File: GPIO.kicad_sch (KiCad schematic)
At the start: 12 parts, among them J10 Conn_01x03_Pin, J11 Conn_01x03_Pin, J12 Conn_01x04_Pin, J13 Conn_01x04_Pin, J14 Conn_01x03_Pin, J78 I2C, J8 Conn_01x03_Pin, J80 I2C, U10 ULC0524P, U12 ULC0524P

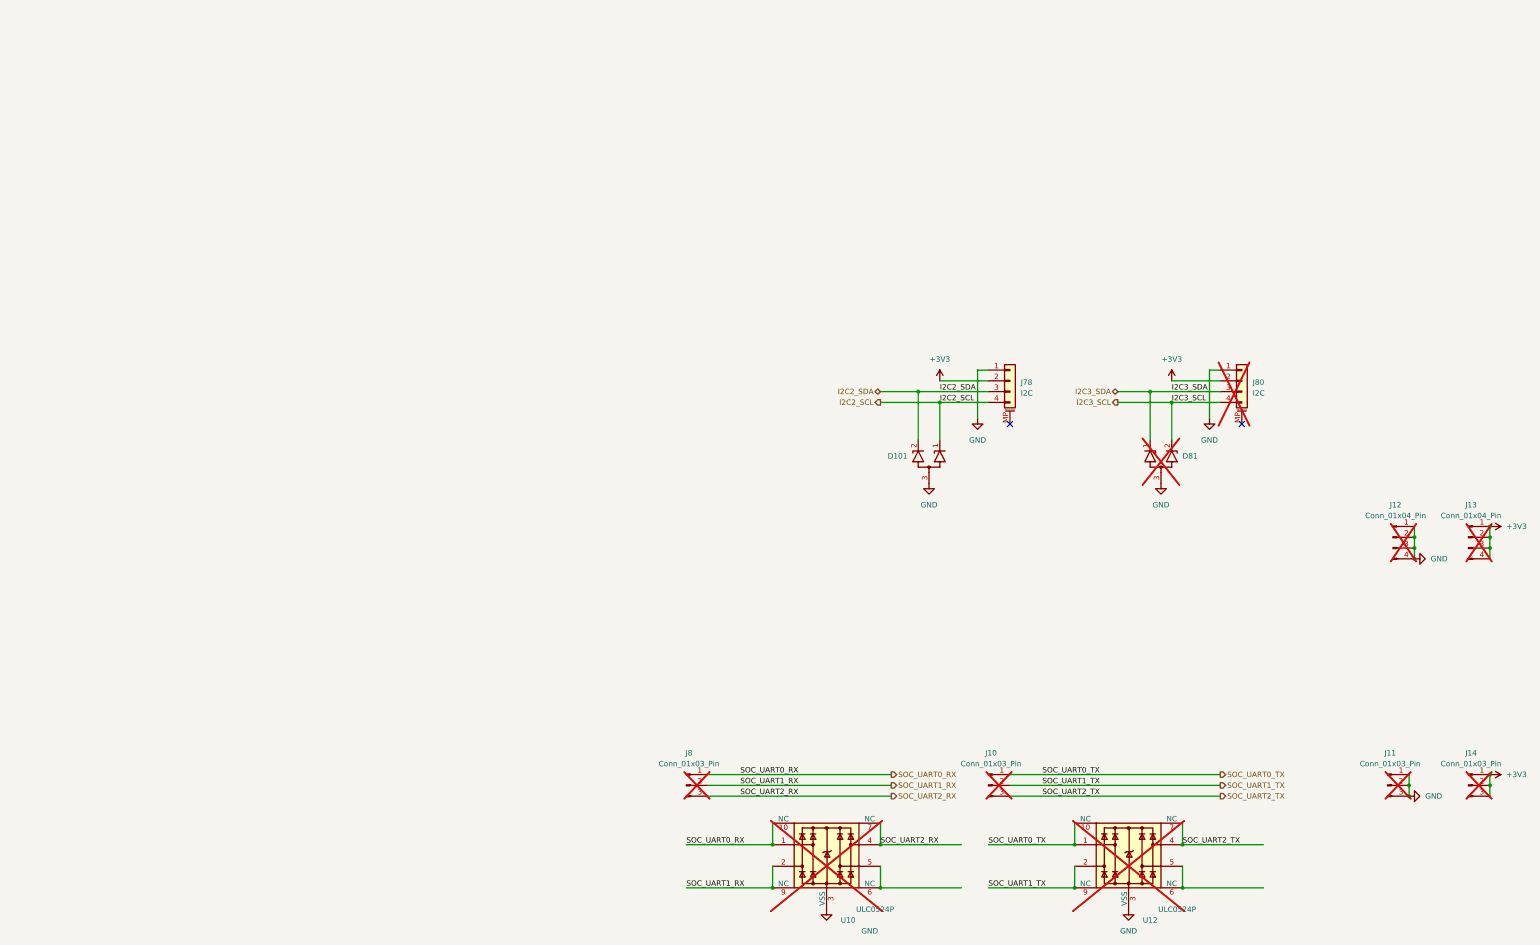
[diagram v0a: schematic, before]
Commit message: hierarchical schema rework
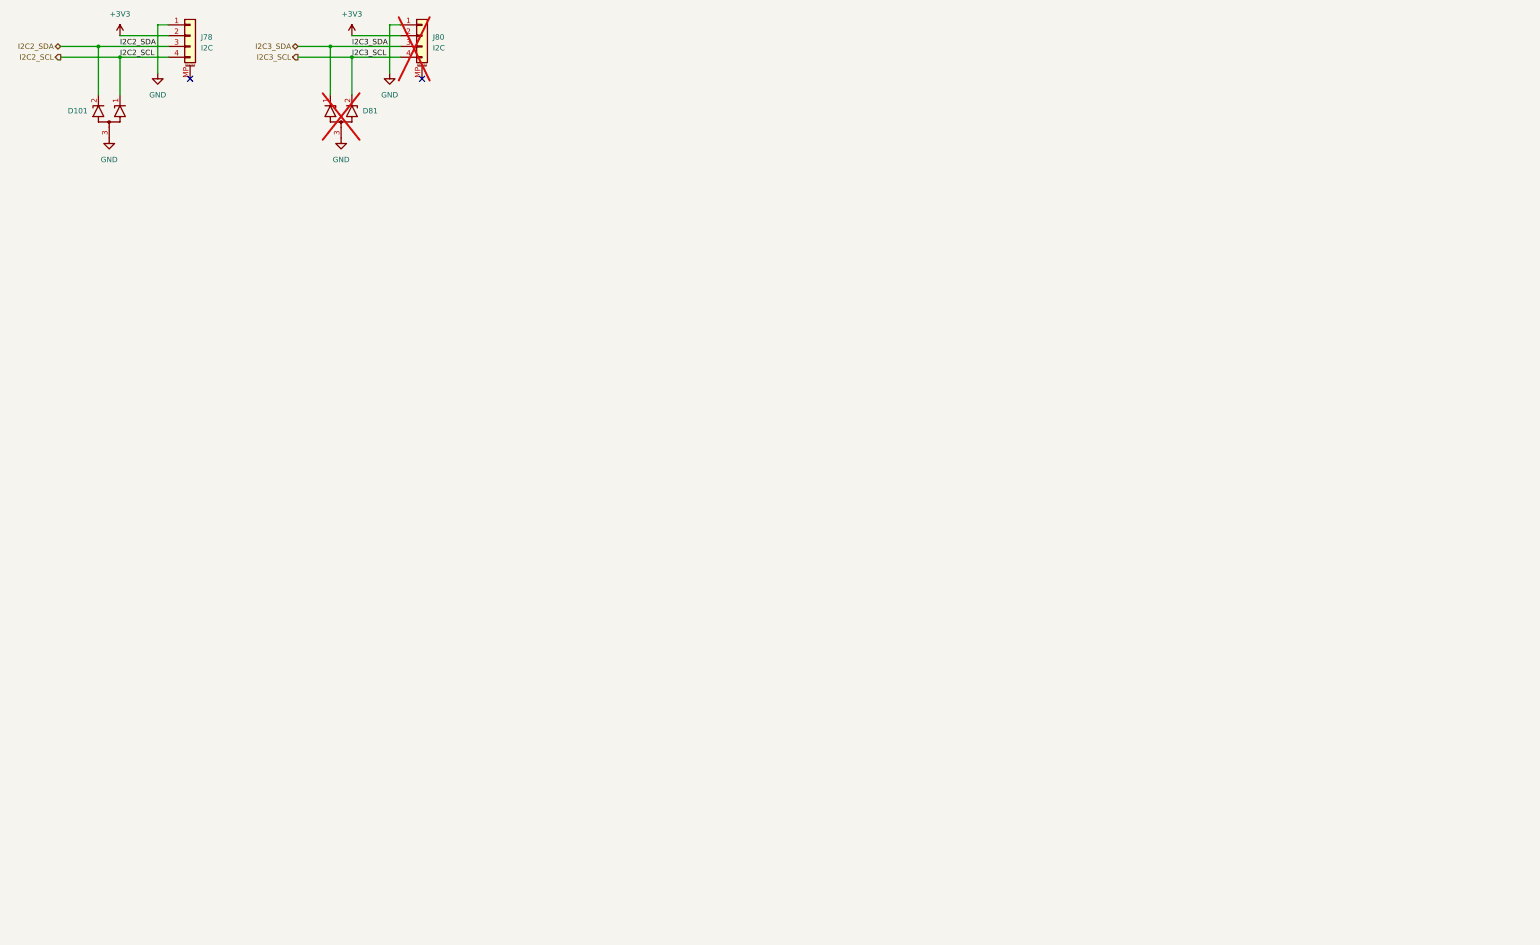
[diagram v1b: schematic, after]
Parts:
- removed J10, J11, J14, J8: Conn_01x03_Pin, A_HDJ_Library:PinHeader_1x03_P2.54mm_Vertical, symbol Connector:Conn_01x03_Pin
- removed J12, J13: Conn_01x04_Pin, A_HDJ_Library:PinHeader_1x04_P2.54mm_Vertical, symbol Connector:Conn_01x04_Pin
- removed U10, U12: ULC0524P, A_HDJ_Library:Diodes_UDFN-10_1.0x2.5mm_P0.5mm, symbol Power_Protection:D3V3XA4B10LP
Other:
- moved on the sheet: D101, D81, J78, J80

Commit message: prod files created
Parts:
- renumbered D101 to D86, D81 to D87, J78 to J81, J80 to J82
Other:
- note added: "[GPIO]"
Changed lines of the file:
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@@
 	(title_block
 		(title "LattePanda_MOKA")
-		(date "2025-12-04")
+		(date "2025-12-14")
 		(rev "1.0")
 		(company "DFRobot")
+	)
+	(text "[GPIO]"
+		(exclude_from_sim no)
+		(at 24.13 17.78 0)
+		(effects
+			(font
+				(face "Arial Black")
+				(size 3.81 3.81)
+			)
+		)
 	)
 	(junction
@@
 		(dnp no)
 		(fields_autoplaced yes)
-		(property "Reference" "#PWR0123"
+		(property "Reference" "#PWR0136"
 			(at 148.59 67.31 0)
 			(effects
@@
 			(project "LattePanda_MOKA"
 				(path "/2a6d114a-7fd7-4207-b5f7-4ea9c34f36aa/f7e36582-0575-4ab7-aed9-3fad0f8951d3"
-					(reference "#PWR0123")
+					(reference "#PWR0136")
 					(unit 1)
 				)
@@
 		(dnp no)
 		(fields_autoplaced yes)
-		(property "Reference" "#PWR098"
+		(property "Reference" "#PWR0138"
 			(at 137.16 82.55 0)
 			(effects
@@
 			(project "LattePanda_MOKA"
 				(path "/2a6d114a-7fd7-4207-b5f7-4ea9c34f36aa/f7e36582-0575-4ab7-aed9-3fad0f8951d3"
-					(reference "#PWR098")
+					(reference "#PWR0138")
 					(unit 1)
 				)
@@
 		(dnp yes)
 		(fields_autoplaced yes)
-		(property "Reference" "D81"
+		(property "Reference" "D87"
 			(at 142.24 69.7865 90)
 			(effects
@@
 			(project "LattePanda_MOKA"
 				(path "/2a6d114a-7fd7-4207-b5f7-4ea9c34f36aa/f7e36582-0575-4ab7-aed9-3fad0f8951d3"
-					(reference "D81")
+					(reference "D87")
 					(unit 1)
 				)
@@
 		(dnp no)
 		(fields_autoplaced yes)
-		(property "Reference" "J78"
+		(property "Reference" "J81"
 			(at 104.14 52.4255 0)
 			(effects
@@
 			(project "LattePanda_MOKA"
 				(path "/2a6d114a-7fd7-4207-b5f7-4ea9c34f36aa/f7e36582-0575-4ab7-aed9-3fad0f8951d3"
-					(reference "J78")
+					(reference "J81")
 					(unit 1)
 				)
@@
 		(dnp no)
 		(fields_autoplaced yes)
-		(property "Reference" "#PWR0122"
+		(property "Reference" "#PWR0134"
 			(at 139.7 55.88 0)
 			(effects
@@
 			(project "LattePanda_MOKA"
 				(path "/2a6d114a-7fd7-4207-b5f7-4ea9c34f36aa/f7e36582-0575-4ab7-aed9-3fad0f8951d3"
-					(reference "#PWR0122")
+					(reference "#PWR0134")
 					(unit 1)
 				)
@@
 		(dnp no)
 		(fields_autoplaced yes)
-		(property "Reference" "#PWR080"
+		(property "Reference" "#PWR0135"
 			(at 93.98 67.31 0)
 			(effects
@@
 			(project "LattePanda_MOKA"
 				(path "/2a6d114a-7fd7-4207-b5f7-4ea9c34f36aa/f7e36582-0575-4ab7-aed9-3fad0f8951d3"
-					(reference "#PWR080")
+					(reference "#PWR0135")
 					(unit 1)
 				)
@@
 		(dnp no)
 		(fields_autoplaced yes)
-		(property "Reference" "#PWR097"
+		(property "Reference" "#PWR0137"
 			(at 82.55 82.55 0)
 			(effects
@@
 			(project "LattePanda_MOKA"
 				(path "/2a6d114a-7fd7-4207-b5f7-4ea9c34f36aa/f7e36582-0575-4ab7-aed9-3fad0f8951d3"
-					(reference "#PWR097")
+					(reference "#PWR0137")
 					(unit 1)
 				)
@@
 		(dnp no)
 		(fields_autoplaced yes)
-		(property "Reference" "#PWR083"
+		(property "Reference" "#PWR0133"
 			(at 85.09 55.88 0)
 			(effects
@@
 			(project "LattePanda_MOKA"
 				(path "/2a6d114a-7fd7-4207-b5f7-4ea9c34f36aa/f7e36582-0575-4ab7-aed9-3fad0f8951d3"
-					(reference "#PWR083")
+					(reference "#PWR0133")
 					(unit 1)
 				)
@@
 		(on_board yes)
 		(dnp no)
-		(property "Reference" "D101"
+		(property "Reference" "D86"
 			(at 77.47 69.7865 90)
 			(effects
@@
 			(project "LattePanda_MOKA"
 				(path "/2a6d114a-7fd7-4207-b5f7-4ea9c34f36aa/f7e36582-0575-4ab7-aed9-3fad0f8951d3"
-					(reference "D101")
+					(reference "D86")
 					(unit 1)
 				)
@@
 		(dnp yes)
 		(fields_autoplaced yes)
-		(property "Reference" "J80"
+		(property "Reference" "J82"
 			(at 158.75 52.4255 0)
 			(effects
@@
 			(project "LattePanda_MOKA"
 				(path "/2a6d114a-7fd7-4207-b5f7-4ea9c34f36aa/f7e36582-0575-4ab7-aed9-3fad0f8951d3"
-					(reference "J80")
+					(reference "J82")
 					(unit 1)
 				)
